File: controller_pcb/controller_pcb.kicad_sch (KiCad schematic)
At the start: 0 parts

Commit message: Imported symbols and footprints
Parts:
- added C1: CL21B106KOQNNNE, CAPC2012X140N, symbol Controller_Comp:CL21B106KOQNNNE
- added IC1: ATTINY85V-10SU, Controller_Footprints:SOIC127P798X216-8N, symbol Controller_Comp:ATTINY85V-10SU
- added R1: ERJP06F1002V, Controller_Footprints:ERJP06D1000V, symbol Controller_Comp:ERJP06F1002V
- added S1: B3F-1050, Controller_Footprints:B3F1000, symbol Controller_Comp:B3F-1050

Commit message: Started placing and wiring
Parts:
- added C2, C3, C4, C5: CL21B106KOQNNNE, CAPC2012X140N, symbol Controller_Comp:CL21B106KOQNNNE
- added R2, R3, R4, R5: ERJP06F1002V, Controller_Footprints:ERJP06D1000V, symbol Controller_Comp:ERJP06F1002V
- added S2, S3, S4, S5: B3F-1050, Controller_Footprints:B3F1000, symbol Controller_Comp:B3F-1050
- added V1: 1, symbol Simulation_SPICE:VDC
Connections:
- net at IC1.1 ((PCINT5/~{RESET}/ADC0/DW)_PB5): now also S1.3, R5.2
- net at IC1.2 ((PCINT3/XTAL1/CLKI/~{OC1B}/ADC3)_PB3): now also R4.2
- net GND: now reaches IC1.4 (GND)
- net at IC1.5 (PB0_(MOSI/DI/SDA/AIN0/OC0A/~{OC1A}/AREF/PCINT0)): now also R1.1
- net at IC1.6 (PB1_(MISO/DO/AIN1/OC0B/OC1A/PCINT1)): now also R2.1
- net at IC1.7 (PB2_(SCK/USCK/SCL/ADC1/T0/INT0/PCINT2)): now also R3.1
- net at R1.2: now also R2.2, R3.2
- new net: R4.1, R5.1, V1.1
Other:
- moved on the sheet: C1, IC1, R1, S1

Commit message: Finished schematic, updating PCB
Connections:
- net GND: now also S1.2, S2.2, S3.1, S4.1, S5.1, V1.2
- net at IC1.2 ((PCINT3/XTAL1/CLKI/~{OC1B}/ADC3)_PB3), R4.2: now also S2.3
- net at IC1.5 (PB0_(MOSI/DI/SDA/AIN0/OC0A/~{OC1A}/AREF/PCINT0)), R1.1: now also S3.4
- net at IC1.6 (PB1_(MISO/DO/AIN1/OC0B/OC1A/PCINT1)), R2.1: now also S4.4
- net at IC1.7 (PB2_(SCK/USCK/SCL/ADC1/T0/INT0/PCINT2)), R3.1: now also S5.4
- net at R4.1, R5.1, V1.1: now also R1.2, R2.2, R3.2
- net at C4.1: now also S4.3
- net at C4.2: now also S4.2
- net at C2.1: now also S2.1
- net at C2.2: now also S2.4
- net at C3.1: now also S3.3
- net at C3.2: now also S3.2
- net at C5.1: now also S5.3
- net at C5.2: now also S5.2
- net at S1.1: now also C1.1
- net at S1.4: now also C1.2
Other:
- moved on the sheet: IC1

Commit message: Placed most components, added mounting holes
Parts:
- removed IC1: ATTINY85V-10SU, Controller_Footprints:SOIC127P798X216-8N, symbol Controller_Comp:ATTINY85V-10SU
- added IC2: ATTINY85-20PU, Controller_Footprints:DIP781W56P254L950H533Q8N, symbol Controller_Comp:ATTINY85-20PU
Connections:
- net GND: now also IC2.4 (GROUND)
- net at R5.2, S1.3: now also IC2.1 (PB5_(PCINT5/~{RESET}/ADC0/DW))
- net at R4.2, S2.3: now also IC2.2 (PB3_(PCINT3/XTAL1/CLKI/~{OC1B}/ADC3))
- net at R1.1, S3.4: now also IC2.5 (PB0_(MOSI/DI/SDA/AIN0/OC0A/OC1A/AREF/PCINT0))
- net at R2.1, S4.4: now also IC2.6 (PB1_(MISO/DO/AIN1/OC0B/OC1A/PCINT1))
- net at R3.1, S5.4: now also IC2.7 (PB2_(SCK/USCK/SCL/ADC1/T0/INT0/PCINT2))
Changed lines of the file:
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@@
-	)
-	(symbol
-		(lib_id "Controller_Comp:ATTINY85V-10SU")
-		(at 99.06 41.91 0)
-		(unit 1)
-		(exclude_from_sim no)
-		(in_bom yes)
-		(on_board yes)
-		(dnp no)
-		(fields_autoplaced yes)
-		(property "Reference" "IC1"
-			(at 151.765 34.29 0)
-			(effects
-				(font
-					(size 1.27 1.27)
-				)
-			)
-		)
-		(property "Value" "ATTINY85V-10SU"
-			(at 151.765 36.83 0)
-			(effects
-				(font
-					(size 1.27 1.27)
-				)
-			)
-		)
-		(property "Footprint" "Controller_Footprints:SOIC127P798X216-8N"
-			(at 214.63 136.83 0)
-			(effects
-				(font
-					(size 1.27 1.27)
-				)
-				(justify left top)
-				(hide yes)
-			)
-		)
-		(property "Datasheet" "https://datasheet.datasheetarchive.com/originals/distributors/Datasheets_SAMA/b7d776087f3438c2ffab22c1216558b5.pdf"
-			(at 214.63 236.83 0)
-			(effects
-				(font
-					(size 1.27 1.27)
-				)
-				(justify left top)
-				(hide yes)
-			)
-		)
-		(property "Description" "ATTINY85V-10SU, 8 bit AVR Microcontroller 10MHz 8kb Flash, 512B RAM, I2C SPI 8-Pin SOIC"
-			(at 152.908 56.388 0)
-			(effects
-				(font
-					(size 1.27 1.27)
-				)
-				(hide yes)
-			)
-		)
-		(property "Height" "2.16"
-			(at 214.63 436.83 0)
-			(effects
-				(font
-					(size 1.27 1.27)
-				)
-				(justify left top)
-				(hide yes)
-			)
-		)
-		(property "Manufacturer_Name" "Microchip"
-			(at 214.63 536.83 0)
-			(effects
-				(font
-					(size 1.27 1.27)
-				)
-				(justify left top)
-				(hide yes)
-			)
-		)
-		(property "Manufacturer_Part_Number" "ATTINY85V-10SU"
-			(at 214.63 636.83 0)
-			(effects
-				(font
-					(size 1.27 1.27)
-				)
-				(justify left top)
-				(hide yes)
-			)
-		)
-		(property "Mouser Part Number" "556-ATTINY85V10SU"
-			(at 214.63 736.83 0)
-			(effects
-				(font
-					(size 1.27 1.27)
-				)
-				(justify left top)
-				(hide yes)
-			)
-		)
-		(property "Mouser Price/Stock" "https://www.mouser.co.uk/ProductDetail/Microchip-Technology/ATTINY85V-10SU?qs=8jWQYweyg6NQ5xH6egcL8w%3D%3D"
-			(at 214.63 836.83 0)
-			(effects
-				(font
-					(size 1.27 1.27)
-				)
-				(justify left top)
-				(hide yes)
-			)
-		)
-		(property "Arrow Part Number" "ATTINY85V-10SU"
-			(at 214.63 936.83 0)
-			(effects
-				(font
-					(size 1.27 1.27)
-				)
-				(justify left top)
-				(hide yes)
-			)
-		)
-		(property "Arrow Price/Stock" "https://www.arrow.com/en/products/attiny85v-10su/microchip-technology?utm_currency=USD&region=nac"
-			(at 214.63 1036.83 0)
-			(effects
-				(font
-					(size 1.27 1.27)
-				)
-				(justify left top)
-				(hide yes)
-			)
-		)
-		(pin "2"
-		)
-		(pin "4"
-		)
-		(pin "7"
-		)
-		(pin "5"
-		)
-		(pin "1"
-		)
-		(pin "3"
-		)
-		(pin "8"
-		)
-		(pin "6"
-		)
-		(instances
-			(project ""
-				(path "/35628871-c2d7-47c8-b610-2ce05008c7f9"
-					(reference "IC1")
-					(unit 1)
-				)
-			)
-		)
 	)
 	(symbol
@@
 					(unit 1)
 				)
+			)
+		)
+	)
+	(symbol
+		(lib_id "Controller_Comp:ATTINY85-20PU")
+		(at 99.06 41.91 0)
+		(unit 1)
+		(exclude_from_sim no)
+		(in_bom yes)
+		(on_board yes)
+		(dnp no)
+		(fields_autoplaced yes)
+		(property "Reference" "IC2"
+			(at 157.48 35.56 0)
+			(effects
+				(font
+					(size 1.27 1.27)
+				)
+			)
+		)
+		(property "Value" "ATTINY85-20PU"
+			(at 157.48 38.1 0)
+			(effects
+				(font
+					(size 1.27 1.27)
+				)
+			)
+		)
+		(property "Footprint" "Controller_Footprints:DIP781W56P254L950H533Q8N"
+			(at 212.09 136.83 0)
+			(effects
+				(font
+					(size 1.27 1.27)
+				)
+				(justify left top)
+			)
+		)
+		(property "Datasheet" "https://componentsearchengine.com/Datasheets/2/ATTINY85-20PU.pdf"
+			(at 212.09 236.83 0)
+			(effects
+				(font
+					(size 1.27 1.27)
+				)
+				(justify left top)
+				(hide yes)
+			)
+		)
+		(property "Description" "MICROCHIP - ATTINY85-20PU - MICROCONTROLLER MCU, 8 BIT, ATTINY, 20MHZ, DIP-8"
+			(at 99.06 41.91 0)
+			(effects
+				(font
+					(size 1.27 1.27)
+				)
+				(hide yes)
+			)
+		)
+		(property "Height" "5.334"
+			(at 212.09 436.83 0)
+			(effects
+				(font
+					(size 1.27 1.27)
+				)
+				(justify left top)
+				(hide yes)
+			)
+		)
+		(property "Manufacturer_Name" "Microchip"
+			(at 212.09 536.83 0)
+			(effects
+				(font
+					(size 1.27 1.27)
+				)
+				(justify left top)
+				(hide yes)
+			)
+		)
+		(property "Manufacturer_Part_Number" "ATTINY85-20PU"
+			(at 212.09 636.83 0)
+			(effects
+				(font
+					(size 1.27 1.27)
+				)
+				(justify left top)
+				(hide yes)
+			)
+		)
+		(property "Mouser Part Number" "556-ATTINY85-20PU"
+			(at 212.09 736.83 0)
+			(effects
+				(font
+					(size 1.27 1.27)
+				)
+				(justify left top)
+				(hide yes)
+			)
+		)
+		(property "Mouser Price/Stock" "https://www.mouser.co.uk/ProductDetail/Microchip-Technology/ATTINY85-20PU?qs=8jWQYweyg6NCiiaOb5GI9Q%3D%3D"
+			(at 212.09 836.83 0)
+			(effects
+				(font
+					(size 1.27 1.27)
+				)
+				(justify left top)
+				(hide yes)
+			)
+		)
+		(property "Arrow Part Number" "ATTINY85-20PU"
+			(at 212.09 936.83 0)
+			(effects
+				(font
+					(size 1.27 1.27)
+				)
+				(justify left top)
+				(hide yes)
+			)
+		)
+		(property "Arrow Price/Stock" "https://www.arrow.com/en/products/attiny85-20pu/microchip-technology?utm_currency=USD&region=nac"
+			(at 212.09 1036.83 0)
+			(effects
+				(font
+					(size 1.27 1.27)
+				)
+				(justify left top)
+				(hide yes)
+			)
+		)
+		(pin "2"
+		)
+		(pin "4"
+		)
+		(pin "6"
+		)
+		(pin "8"
+		)
+		(pin "5"
+		)
+		(pin "7"
+		)
+		(pin "3"
+		)
+		(pin "1"
+		)
+		(instances
+			(project ""
+				(path "/35628871-c2d7-47c8-b610-2ce05008c7f9"
+					(reference "IC2")
+					(unit 1)
+				)

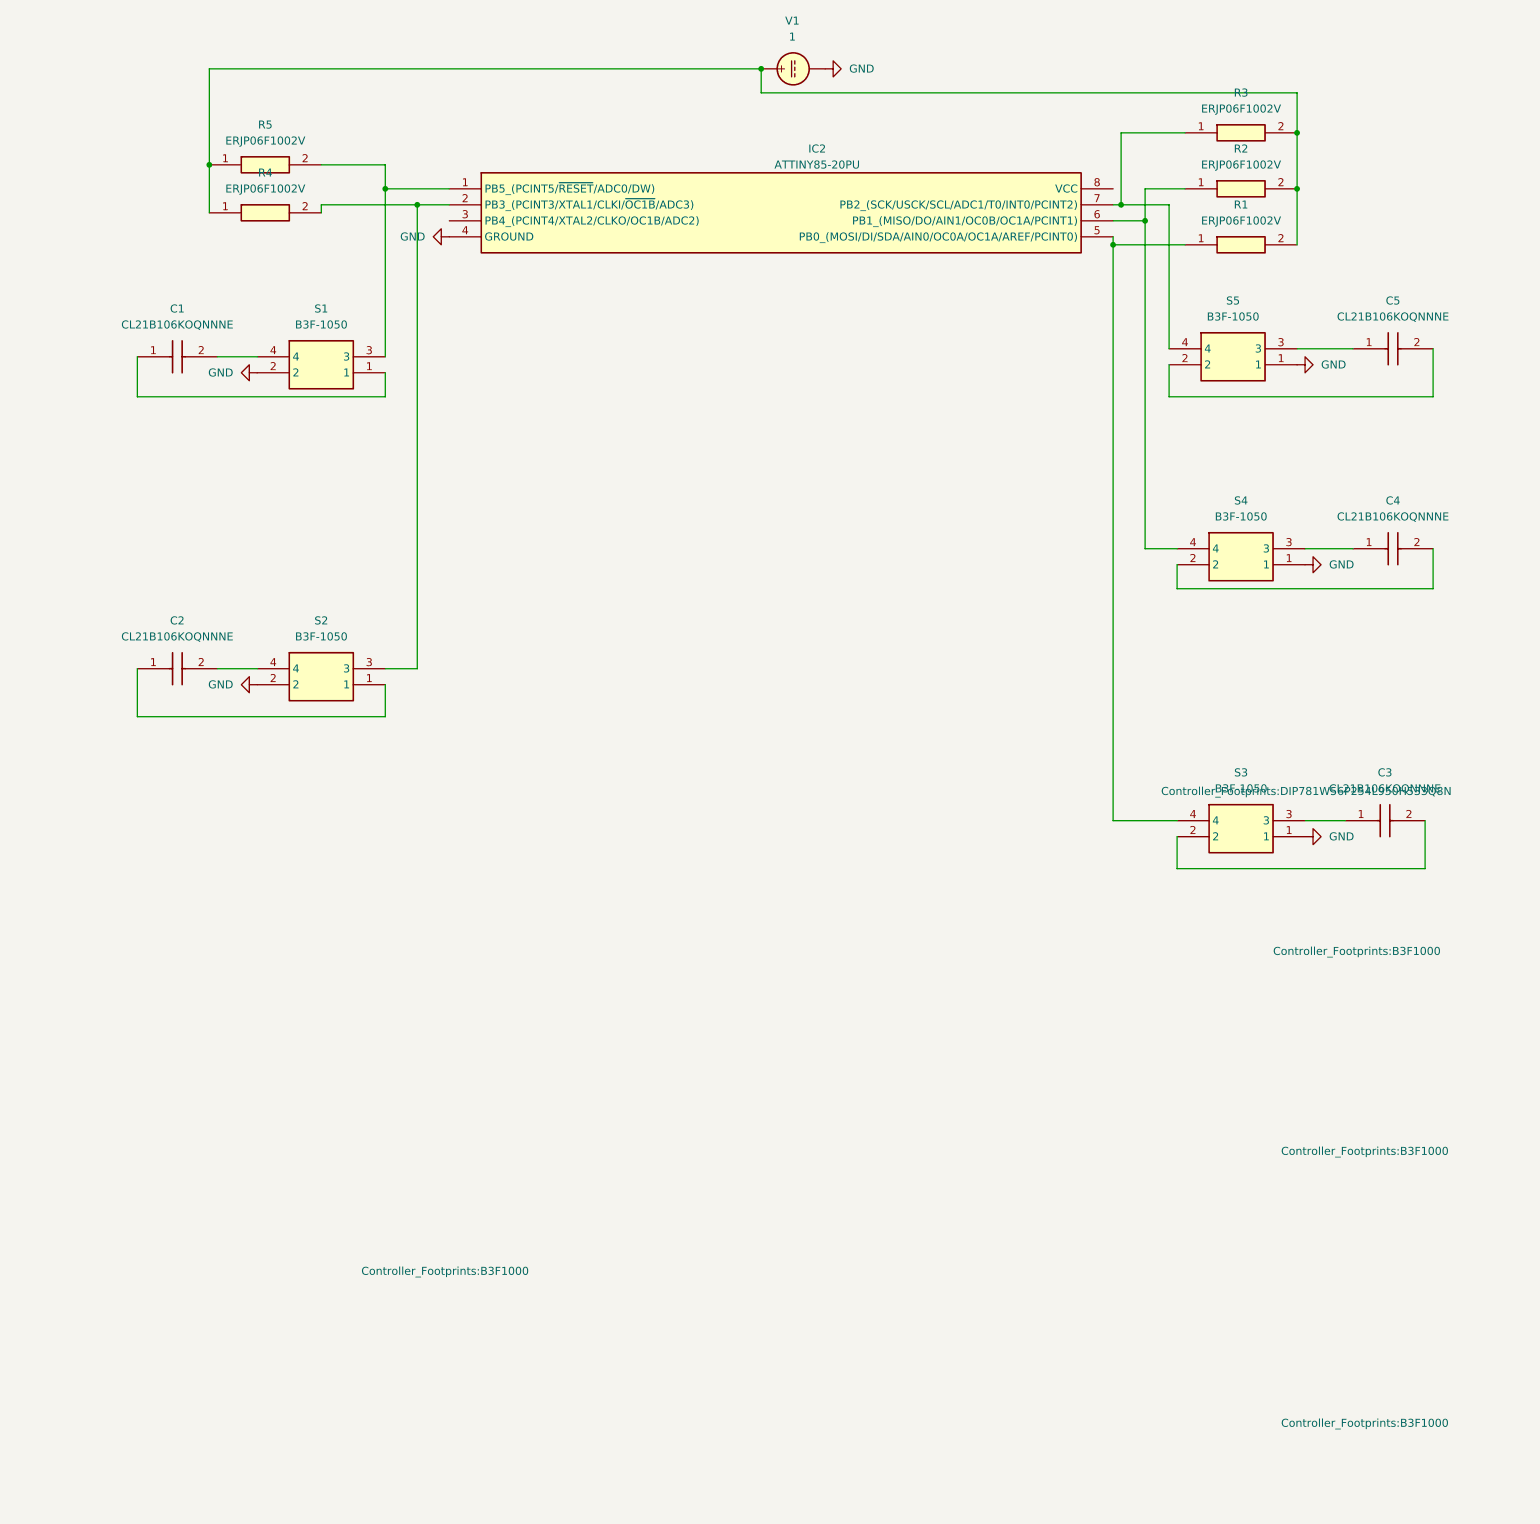
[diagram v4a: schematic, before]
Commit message: Replaced voltage regulator, added 3D files
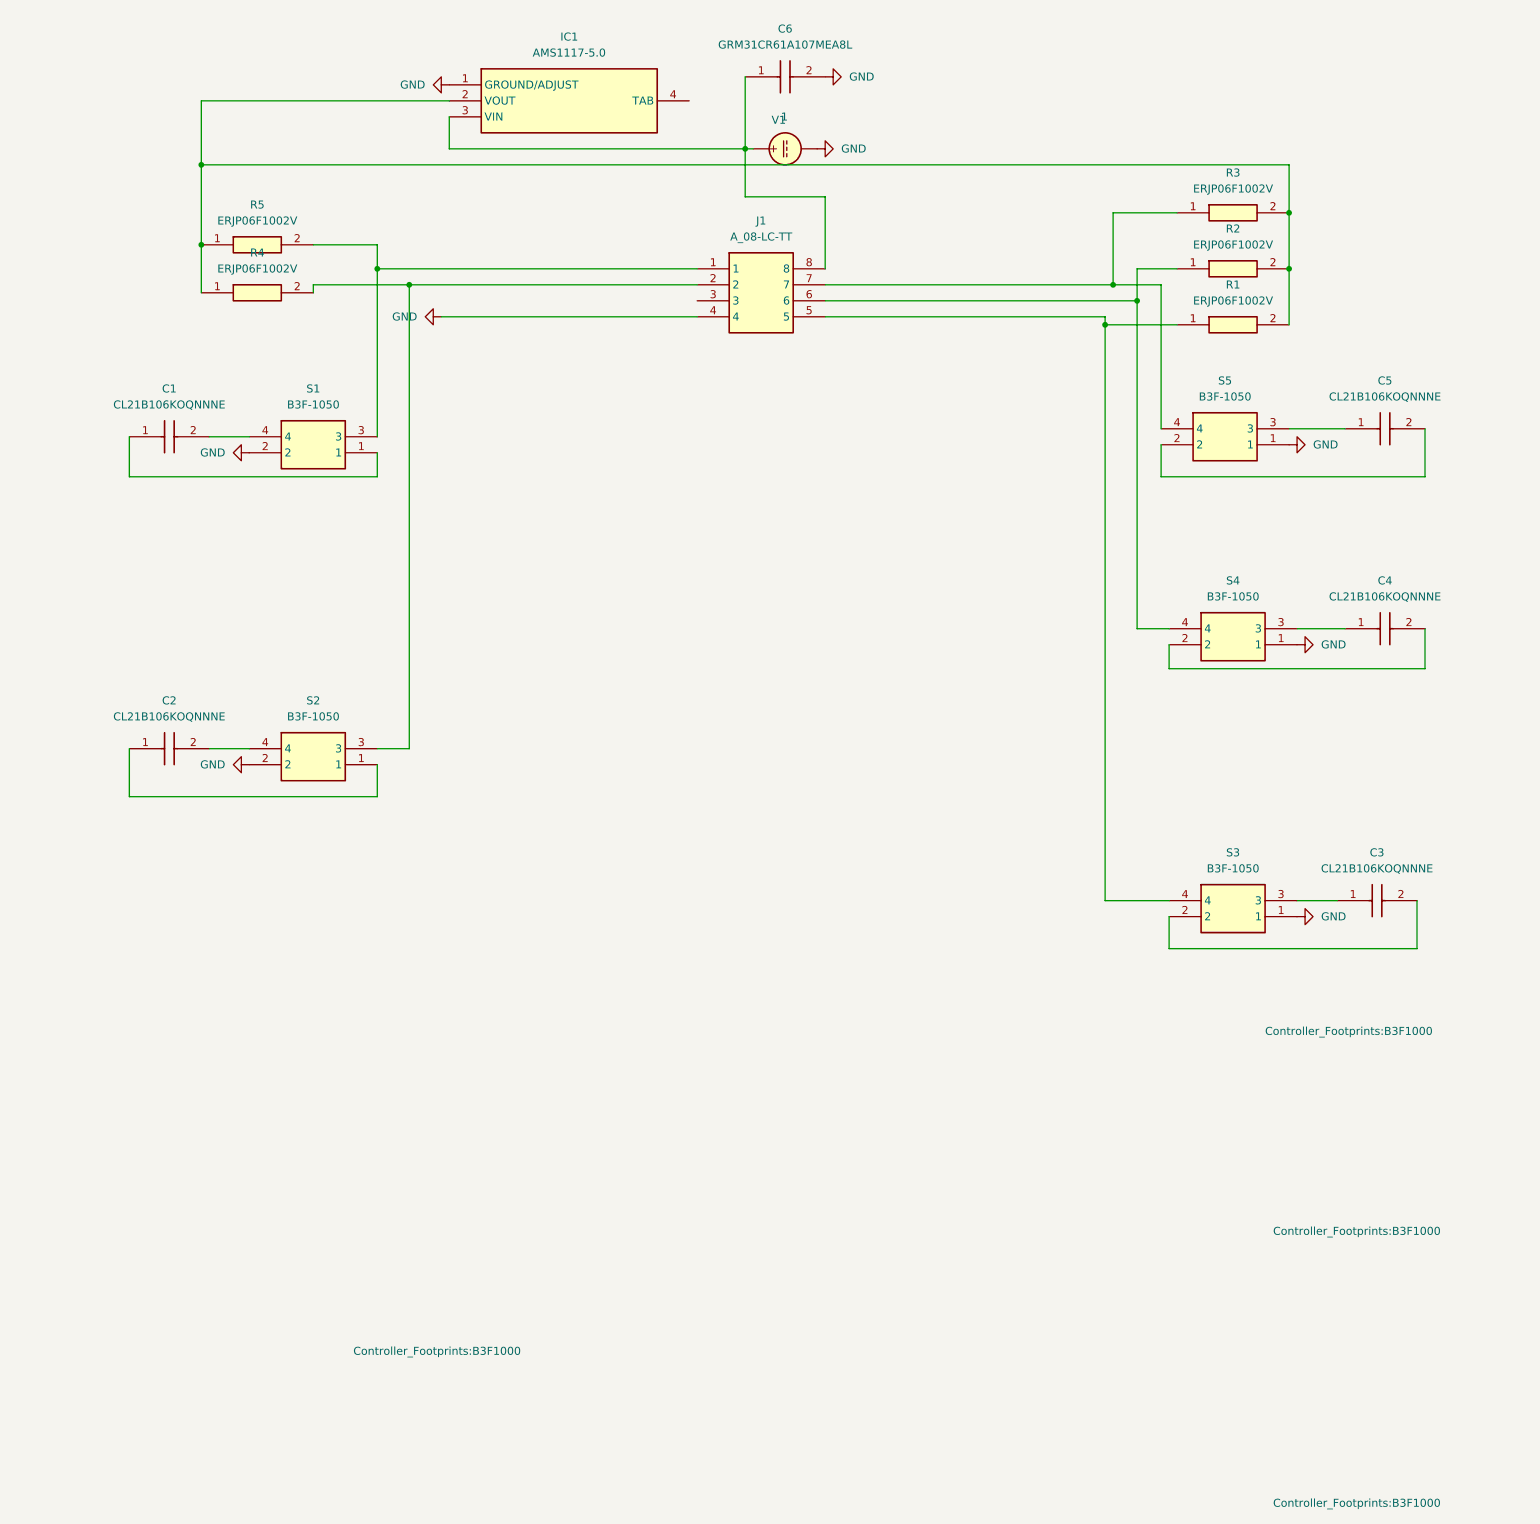
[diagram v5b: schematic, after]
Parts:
- removed IC2: ATTINY85-20PU, Controller_Footprints:DIP781W56P254L950H533Q8N, symbol Controller_Comp:ATTINY85-20PU
- added C6: GRM31CR61A107MEA8L, GRM31x, symbol Controller_Comp:GRM31CR61A107MEA8L
- added IC1: AMS1117-5.0, Controller_Footprints:SOT229P700X180-4N, symbol Controller_Comp:AMS1117-5.0
- added J1: A_08-LC-TT, Controller_Footprints:DIPS762W61P254L1016H525Q8N, symbol Controller_Comp:A_08-LC-TT
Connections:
- net GND: now also C6.2, IC1.1 (GROUND/ADJUST), J1.4
- net at R1.2, R2.2, R3.2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: now also IC1.2 (VOUT); no longer V1.1
- net at R4.2, S2.3: now also J1.2
- net at R5.2, S1.3: now also J1.1
- net at R2.1, S4.4: now also J1.6
- net at R3.1, S5.4: now also J1.7
- net at R1.1, S3.4: now also J1.5
- new net: C6.1, IC1.3 (VIN), J1.8, V1.1
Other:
- moved on the sheet: C1, C2, C3, C4, C5, R1, R2, R3, R4, R5, S1, S2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
